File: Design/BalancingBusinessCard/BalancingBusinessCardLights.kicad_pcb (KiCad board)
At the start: 2 copper layers, 51 x 89 mm, 41 parts, among them J1 Conn_02x01, U1 ATtiny261A-MU, U2 LIS3DHTR, U3 MCP1640DCH

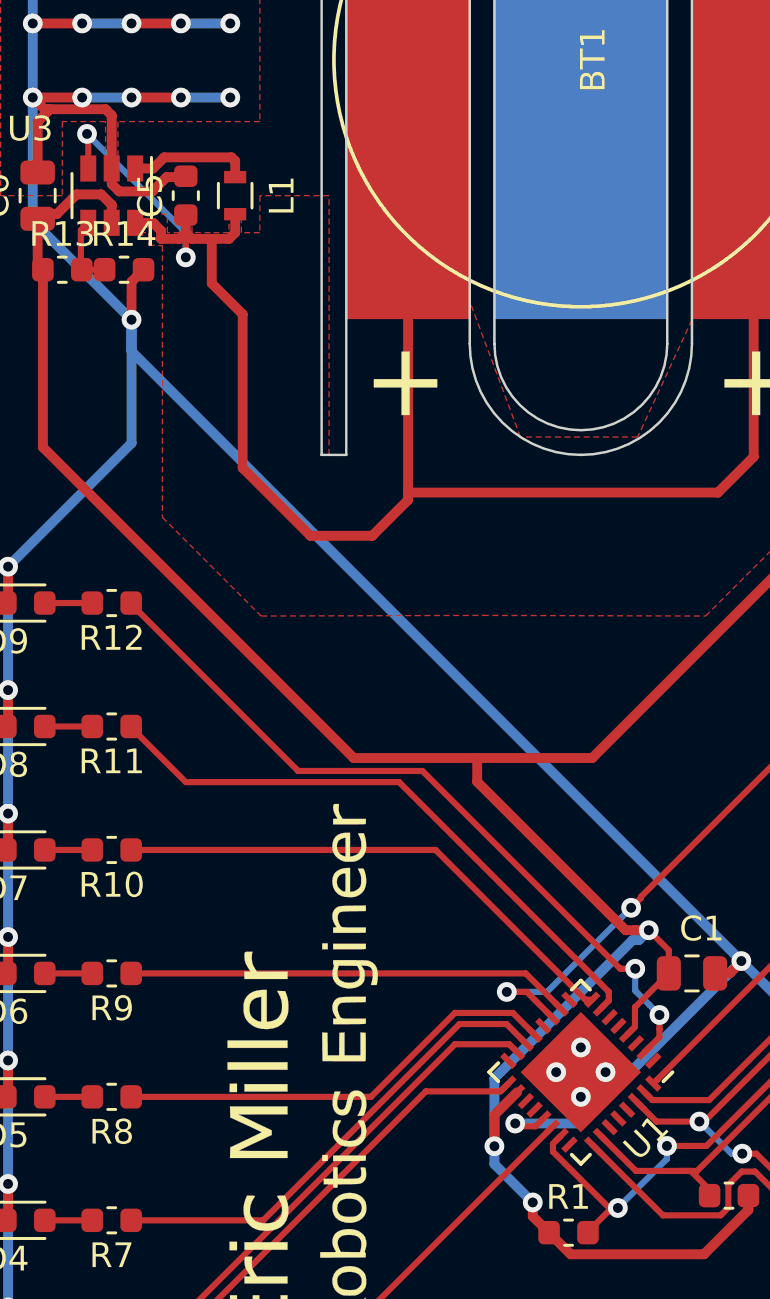
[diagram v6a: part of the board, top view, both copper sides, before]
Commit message: Minor DRC fixes
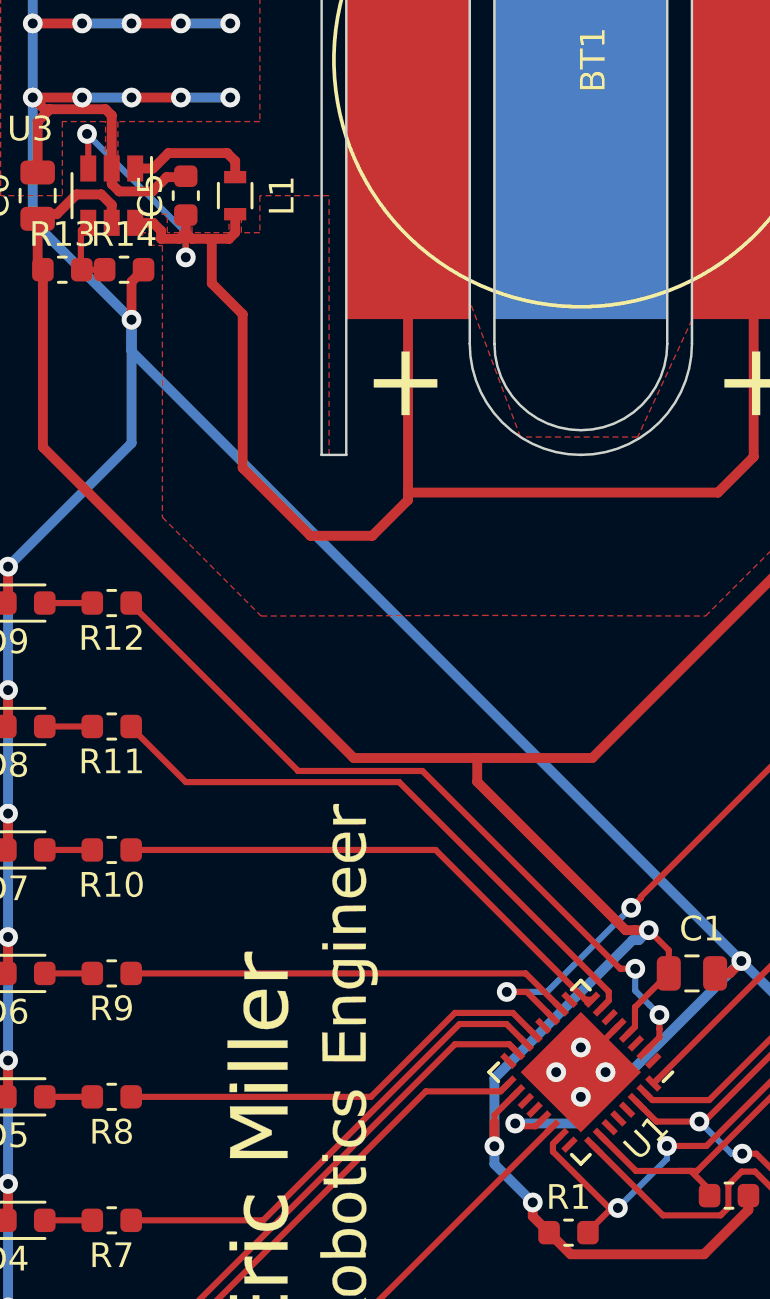
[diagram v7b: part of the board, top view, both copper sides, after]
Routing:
- net GND: track 309.6 -> 311.4 mm
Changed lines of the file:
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@@
     (thickness 1.6)
     (drawings 36)
-    (tracks 380)
+    (tracks 383)
     (zones 0)
     (modules 41)
@@
   (segment (start 231.75 55.75) (end 230 55.75) (width 0.25) (layer B.Cu) (net 2))
   (segment (start 232.75 56.75) (end 231.75 55.75) (width 0.25) (layer B.Cu) (net 2))
+  (segment (start 211.064007 115.25403) (end 210.197801 115.25403) (width 0.25) (layer F.Cu) (net 2))
+  (segment (start 211.718081 114.599956) (end 211.064007 115.25403) (width 0.25) (layer F.Cu) (net 2))
   (segment (start 206.945111 117.251605) (end 207.263308 116.933408) (width 0.25) (layer F.Cu) (net 3) (status 20))
   (segment (start 203.919985 117.251605) (end 206.945111 117.251605) (width 0.25) (layer F.Cu) (net 3))
@@
   (segment (start 212.547802 111.123788) (end 212.297802 111.123788) (width 0.4) (layer B.Cu) (net 13))
   (via (at 212.947801 110.723789) (size 0.8) (drill 0.4) (layers F.Cu B.Cu) (net 13))
-  (segment (start 206.697801 118.206022) (end 206.697801 119.473789) (width 0.4) (layer F.Cu) (net 13))
-  (segment (start 207.616861 117.286962) (end 206.697801 118.206022) (width 0.4) (layer F.Cu) (net 13) (status 10))
   (segment (start 213.760301 112.473789) (end 213.760301 111.536289) (width 0.25) (layer F.Cu) (net 13) (status 10))
   (segment (start 213.760301 111.536289) (end 212.947801 110.723789) (width 0.25) (layer F.Cu) (net 13))
@@
   (segment (start 226.657801 87.751882) (end 226.657801 85.27587) (width 0.4) (layer F.Cu) (net 13))
   (segment (start 226.657801 85.27587) (end 226.657801 84.073789) (width 0.4) (layer F.Cu) (net 13))
-  (segment (start 190.447801 137.473789) (end 188.485301 137.473789) (width 0.25) (layer F.Cu) (net 20) (status 30))
-  (segment (start 190.447801 132.473789) (end 188.485301 132.473789) (width 0.25) (layer F.Cu) (net 21) (status 30))
-  (segment (start 190.447801 127.473789) (end 188.485301 127.473789) (width 0.25) (layer F.Cu) (net 22) (status 30))
-  (segment (start 190.447801 122.473789) (end 188.485301 122.473789) (width 0.25) (layer F.Cu) (net 23) (status 30))
-  (segment (start 190.447801 117.473789) (end 188.485301 117.473789) (width 0.25) (layer F.Cu) (net 24) (status 30))
-  (segment (start 190.447801 112.473789) (end 188.485301 112.473789) (width 0.25) (layer F.Cu) (net 25) (status 30))
-  (segment (start 190.447801 107.473789) (end 188.485301 107.473789) (width 0.25) (layer F.Cu) (net 26) (status 30))
-  (segment (start 190.447801 102.473789) (end 188.485301 102.473789) (width 0.25) (layer F.Cu) (net 27) (status 30))
-  (segment (start 190.447801 97.473789) (end 188.485301 97.473789) (width 0.25) (layer F.Cu) (net 28) (status 30))
-  (segment (start 190.947801 83.973789) (end 189.947801 83.973789) (width 0.25) (layer F.Cu) (net 30) (status 30))
-  (segment (start 189.947801 82.373789) (end 190.247801 82.073789) (width 0.25) (layer F.Cu) (net 30) (status 30))
-  (segment (start 189.947801 83.973789) (end 189.947801 82.373789) (width 0.25) (layer F.Cu) (net 30) (status 30))
+  (segment (start 206.697801 118.206022) (end 206.697801 118.5) (width 0.25) (layer F.Cu) (net 13))
+  (segment (start 207.616861 117.286962) (end 206.697801 118.206022) (width 0.25) (layer F.Cu) (net 13))
+  (segment (start 206.697801 118.5) (end 206.697801 119.473789) (width 0.4) (layer F.Cu) (net 13))
   (via (at 215 118.473759) (size 0.8) (drill 0.4) (layers F.Cu B.Cu) (net 14))
   (segment (start 216.301231 119.77499) (end 216.737293 119.77499) (width 0.25) (layer B.Cu) (net 14))
@@
   (segment (start 229.197801 77.573789) (end 230.822813 79.198801) (width 0.25) (layer F.Cu) (net 15))
   (segment (start 225.175033 107.824967) (end 215.394841 117.605159) (width 0.25) (layer F.Cu) (net 15))
-  (segment (start 192.872801 79.873789) (end 192.147801 79.873789) (width 0.4) (layer F.Cu) (net 29) (status 20))
-  (segment (start 193.322802 79.423788) (end 192.872801 79.873789) (width 0.4) (layer F.Cu) (net 29))
-  (segment (start 196.0478 79.423788) (end 193.322802 79.423788) (width 0.4) (layer F.Cu) (net 29))
-  (segment (start 196.197801 79.573789) (end 196.0478 79.423788) (width 0.4) (layer F.Cu) (net 29))
-  (segment (start 196.197801 80.223789) (end 196.197801 79.573789) (width 0.4) (layer F.Cu) (net 29) (status 10))
   (segment (start 212.430034 120.473789) (end 211.010974 119.054729) (width 0.25) (layer F.Cu) (net 16) (status 20))
   (segment (start 214.197801 120.473789) (end 212.430034 120.473789) (width 0.25) (layer F.Cu) (net 16))
@@
   (segment (start 216.715096 120.5) (end 216.172811 121.042285) (width 0.25) (layer F.Cu) (net 19))
   (segment (start 218.049989 121.294483) (end 217.255506 120.5) (width 0.25) (layer F.Cu) (net 19))
+  (segment (start 190.447801 137.473789) (end 188.485301 137.473789) (width 0.25) (layer F.Cu) (net 20) (status 30))
+  (segment (start 190.447801 132.473789) (end 188.485301 132.473789) (width 0.25) (layer F.Cu) (net 21) (status 30))
+  (segment (start 190.447801 127.473789) (end 188.485301 127.473789) (width 0.25) (layer F.Cu) (net 22) (status 30))
+  (segment (start 190.447801 122.473789) (end 188.485301 122.473789) (width 0.25) (layer F.Cu) (net 23) (status 30))
+  (segment (start 190.447801 117.473789) (end 188.485301 117.473789) (width 0.25) (layer F.Cu) (net 24) (status 30))
+  (segment (start 190.447801 112.473789) (end 188.485301 112.473789) (width 0.25) (layer F.Cu) (net 25) (status 30))
+  (segment (start 190.447801 107.473789) (end 188.485301 107.473789) (width 0.25) (layer F.Cu) (net 26) (status 30))
+  (segment (start 190.447801 102.473789) (end 188.485301 102.473789) (width 0.25) (layer F.Cu) (net 27) (status 30))
+  (segment (start 190.447801 97.473789) (end 188.485301 97.473789) (width 0.25) (layer F.Cu) (net 28) (status 30))
+  (segment (start 192.872801 79.873789) (end 192.147801 79.873789) (width 0.4) (layer F.Cu) (net 29))
+  (segment (start 193.49659 79.25) (end 192.872801 79.873789) (width 0.4) (layer F.Cu) (net 29))
+  (segment (start 195.874012 79.25) (end 193.49659 79.25) (width 0.4) (layer F.Cu) (net 29))
+  (segment (start 196.197801 80.223789) (end 196.197801 79.573789) (width 0.4) (layer F.Cu) (net 29))
+  (segment (start 196.197801 79.573789) (end 195.874012 79.25) (width 0.4) (layer F.Cu) (net 29))
+  (segment (start 190.947801 83.973789) (end 189.947801 83.973789) (width 0.25) (layer F.Cu) (net 30) (status 30))
+  (segment (start 189.947801 82.373789) (end 190.247801 82.073789) (width 0.25) (layer F.Cu) (net 30) (status 30))
+  (segment (start 189.947801 83.973789) (end 189.947801 82.373789) (width 0.25) (layer F.Cu) (net 30) (status 30))
   (zone (net 13) (net_name +3V3) (layer F.Cu) (hatch edge 0.508)
     (connect_pads (clearance 0.508))

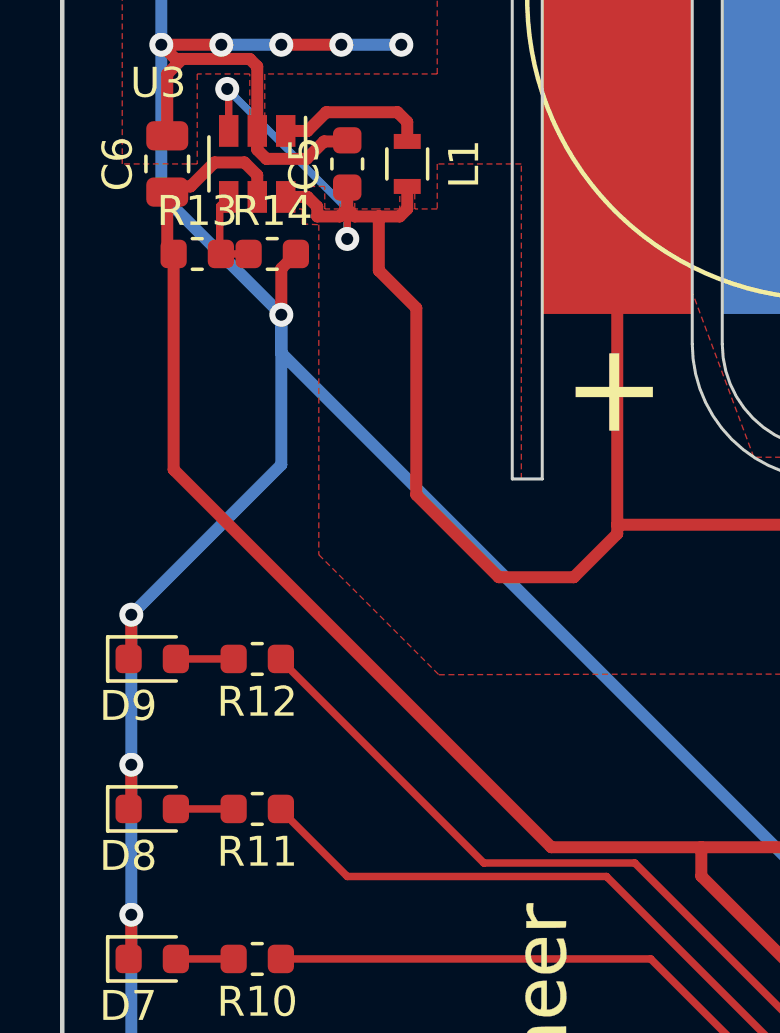
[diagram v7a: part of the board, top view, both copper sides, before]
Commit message: Updated names
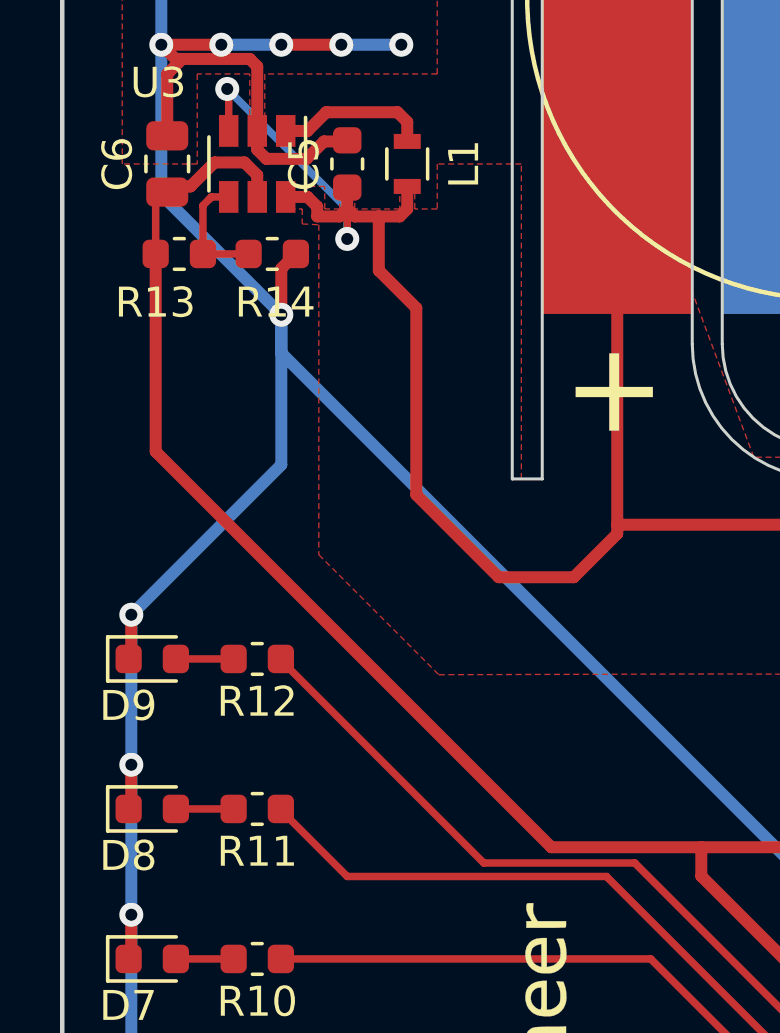
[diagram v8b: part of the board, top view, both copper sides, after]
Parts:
- BT1: value Battery -> CR-2016
- ICSP1: value Conn_02x03_Odd_Even -> ICSP
- J1: value Conn_02x01 -> PWR
- U1: value ATtiny261A-MU -> ATTINY861-15MZ
- U3: value MCP1640DCH -> MCP1640DT-I/CHY
- moved R13 0.60 mm to (188.6, 84.0)
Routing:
- net Net-(R13-Pad2): track 3.02 -> 4.24 mm
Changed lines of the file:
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@@
-(kicad_pcb (version 20171130) (host pcbnew 5.0.2-bee76a0~70~ubuntu18.04.1)
+(kicad_pcb (version 20171130) (host pcbnew 5.1.0-unknown-3692c51~82~ubuntu16.04.1)
   (general
     (thickness 1.6)
     (drawings 36)
-    (tracks 383)
+    (tracks 385)
     (zones 0)
     (modules 41)
@@
   )
   (setup
-    (last_trace_width 0.25)
+    (last_trace_width 0.4)
     (user_trace_width 0.4)
     (user_trace_width 3)
@@
     (zone_45_only no)
     (trace_min 0.2)
-    (segment_width 0.15)
-    (edge_width 0.15)
     (via_size 0.8)
     (via_drill 0.4)
@@
     (uvia_min_size 0.2)
     (uvia_min_drill 0.1)
+    (edge_width 0.15)
+    (segment_width 0.15)
     (pcb_text_width 0.3)
     (pcb_text_size 1.5 1.5)
@@
       (effects (font (size 1 1) (thickness 0.15)))
     )
-    (fp_text value Battery (at 0 -0.5 90) (layer F.Fab)
+    (fp_text value CR-2016 (at 0 -0.5 90) (layer F.Fab)
       (effects (font (size 1 1) (thickness 0.15)))
     )
@@
       (effects (font (size 1 1) (thickness 0.15)))
     )
-    (fp_text value Conn_02x03_Odd_Even (at 1.27 7.41 180) (layer F.Fab)
+    (fp_text value ICSP (at 1.27 7.41 180) (layer F.Fab)
       (effects (font (size 1 1) (thickness 0.15)))
     )
@@
       (effects (font (size 1 1) (thickness 0.15)))
     )
-    (fp_text value ATtiny261A-MU (at 0 3.75 225) (layer F.Fab)
+    (fp_text value ATTINY861-15MZ (at 0 3.75 225) (layer F.Fab)
       (effects (font (size 1 1) (thickness 0.15)))
     )
@@
       (effects (font (size 1 1) (thickness 0.15)))
     )
-    (fp_text value MCP1640DCH (at 0 2.9 270) (layer F.Fab)
+    (fp_text value MCP1640DT-I/CHY (at 0 2.9 270) (layer F.Fab)
       (effects (font (size 1 1) (thickness 0.15)))
     )
@@
       (effects (font (size 1 1) (thickness 0.15)))
     )
-    (fp_text value Conn_02x01 (at 0 4.87 270) (layer F.Fab)
+    (fp_text value PWR (at 0 4.87 270) (layer F.Fab)
       (effects (font (size 1 1) (thickness 0.15)))
     )
@@
   )
   (module Resistor_SMD:R_0603_1608Metric (layer F.Cu)
-    (at 189.197801 83.973789)
+    (at 188.6 83.973789)
     (descr "Resistor SMD 0603 (1608 Metric), square (rectangular) end terminal, IPC_7351 nominal, (Body size source: http://www.tortai-tech.com/upload/download/2011102023233369053.pdf), generated with kicad-footprint-generator")
     (tags resistor)
     (attr smd)
-    (fp_text reference R13 (at 0 -1.43) (layer F.SilkS)
+    (fp_text reference R13 (at -0.797801 1.626211) (layer F.SilkS)
       (effects (font (size 1 1) (thickness 0.15)))
     )
@@
     (tags resistor)
     (attr smd)
-    (fp_text reference R14 (at 0 -1.43) (layer F.SilkS)
+    (fp_text reference R14 (at 0.102199 1.626211) (layer F.SilkS)
       (effects (font (size 1 1) (thickness 0.15)))
     )
@@
   (segment (start 213.760301 112.473789) (end 213.760301 111.536289) (width 0.25) (layer F.Cu) (net 13) (status 10))
   (segment (start 213.760301 111.536289) (end 212.947801 110.723789) (width 0.25) (layer F.Cu) (net 13))
-  (segment (start 188.197801 83.761289) (end 188.410301 83.973789) (width 0.4) (layer F.Cu) (net 13))
-  (segment (start 188.197801 81.911289) (end 188.197801 83.761289) (width 0.4) (layer F.Cu) (net 13))
-  (segment (start 188.410301 91.160301) (end 201 103.75) (width 0.4) (layer F.Cu) (net 13))
-  (segment (start 188.410301 83.973789) (end 188.410301 91.160301) (width 0.4) (layer F.Cu) (net 13))
   (segment (start 206 104.713488) (end 212.010301 110.723789) (width 0.4) (layer F.Cu) (net 13))
   (segment (start 206 103.75) (end 206 104.713488) (width 0.4) (layer F.Cu) (net 13))
-  (segment (start 201 103.75) (end 206 103.75) (width 0.4) (layer F.Cu) (net 13))
   (segment (start 212.382116 110.723789) (end 212.947801 110.723789) (width 0.4) (layer F.Cu) (net 13))
   (segment (start 212.010301 110.723789) (end 212.382116 110.723789) (width 0.4) (layer F.Cu) (net 13))
@@
   (segment (start 207.616861 117.286962) (end 206.697801 118.206022) (width 0.25) (layer F.Cu) (net 13))
   (segment (start 206.697801 118.5) (end 206.697801 119.473789) (width 0.4) (layer F.Cu) (net 13))
+  (segment (start 187.8125 82.29659) (end 188.197801 81.911289) (width 0.25) (layer F.Cu) (net 13))
+  (segment (start 187.8125 83.973789) (end 187.8125 82.29659) (width 0.25) (layer F.Cu) (net 13))
+  (segment (start 201 103.75) (end 206 103.75) (width 0.4) (layer F.Cu) (net 13))
+  (segment (start 187.8125 90.5625) (end 201 103.75) (width 0.4) (layer F.Cu) (net 13))
+  (segment (start 187.8125 83.973789) (end 187.8125 90.5625) (width 0.4) (layer F.Cu) (net 13))
   (via (at 215 118.473759) (size 0.8) (drill 0.4) (layers F.Cu B.Cu) (net 14))
   (segment (start 216.301231 119.77499) (end 216.737293 119.77499) (width 0.25) (layer B.Cu) (net 14))
@@
   (segment (start 196.197801 80.223789) (end 196.197801 79.573789) (width 0.4) (layer F.Cu) (net 29))
   (segment (start 196.197801 79.573789) (end 195.874012 79.25) (width 0.4) (layer F.Cu) (net 29))
-  (segment (start 190.947801 83.973789) (end 189.947801 83.973789) (width 0.25) (layer F.Cu) (net 30) (status 30))
-  (segment (start 189.947801 82.373789) (end 190.247801 82.073789) (width 0.25) (layer F.Cu) (net 30) (status 30))
-  (segment (start 189.947801 83.973789) (end 189.947801 82.373789) (width 0.25) (layer F.Cu) (net 30) (status 30))
+  (segment (start 189.672801 82.073789) (end 189.5875 82.15909) (width 0.25) (layer F.Cu) (net 30))
+  (segment (start 190.247801 82.073789) (end 189.672801 82.073789) (width 0.25) (layer F.Cu) (net 30))
+  (segment (start 189.3875 82.35909) (end 189.3875 83.973789) (width 0.25) (layer F.Cu) (net 30))
+  (segment (start 189.672801 82.073789) (end 189.3875 82.35909) (width 0.25) (layer F.Cu) (net 30))
+  (segment (start 189.3875 83.973789) (end 190.910301 83.973789) (width 0.25) (layer F.Cu) (net 30))
   (zone (net 13) (net_name +3V3) (layer F.Cu) (hatch edge 0.508)
     (connect_pads (clearance 0.508))
